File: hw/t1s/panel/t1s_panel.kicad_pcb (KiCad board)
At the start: 6 copper layers, 70 x 81 mm, 606 parts, among them J1 SFP edge (INF-8074i), J2 S2B-PH-K-S, U1 GW5AT-LV15MG132C1/I0, U2 GD25Q64CWIGR, U3 TPS62822DLC, U4 TPS22918DBVR, U5 LAN8670C2-E/LMX, U6 TLV75518PDBVR, U7 TLV75512PDBVR, U8 STM32G031F6P6, X1 OB2EL89CLIB112YLC-125M, Y1 25MHz CL12pF 2016

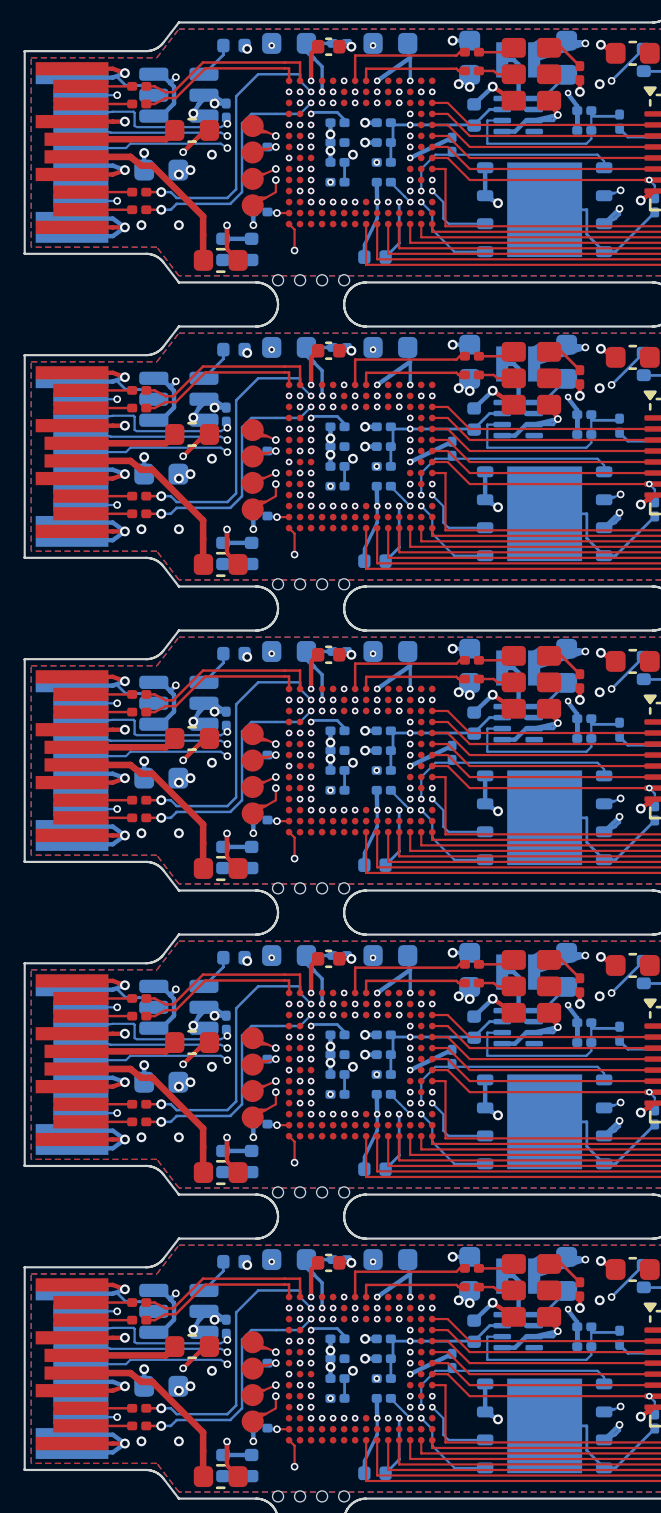
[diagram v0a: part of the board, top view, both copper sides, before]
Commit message: Review fixes: 100 V MDI DC block, 128 Mbit flash, T1S MDI geometry
- T1 C33/C34: 100 nF 100 V X5R 0402 (GRM155R62A104KE14D, C162178), split
  from the 16 V decap line (C1525) they had been grouped with
- T1 R6/R7: 1 k 1 % 0.2 W anti-surge 0402 (C313354) instead of 62.5 mW;
  still short of TI's 0.75 W 2010, documented
- T1S U2: GD25Q128EWIGR (C2982923), same WSON-8 footprint, so Gowin's
  default golden address 0x800000 is inside the part; ORDER.md gives the
  flash layout
- compliance.py: each lane's geometry comes from its routed track width;
  the T1S MDI is two 0.2 mm lines (Z0 44.8) with its own delay and loss,
  and an unsolved width now stops the run
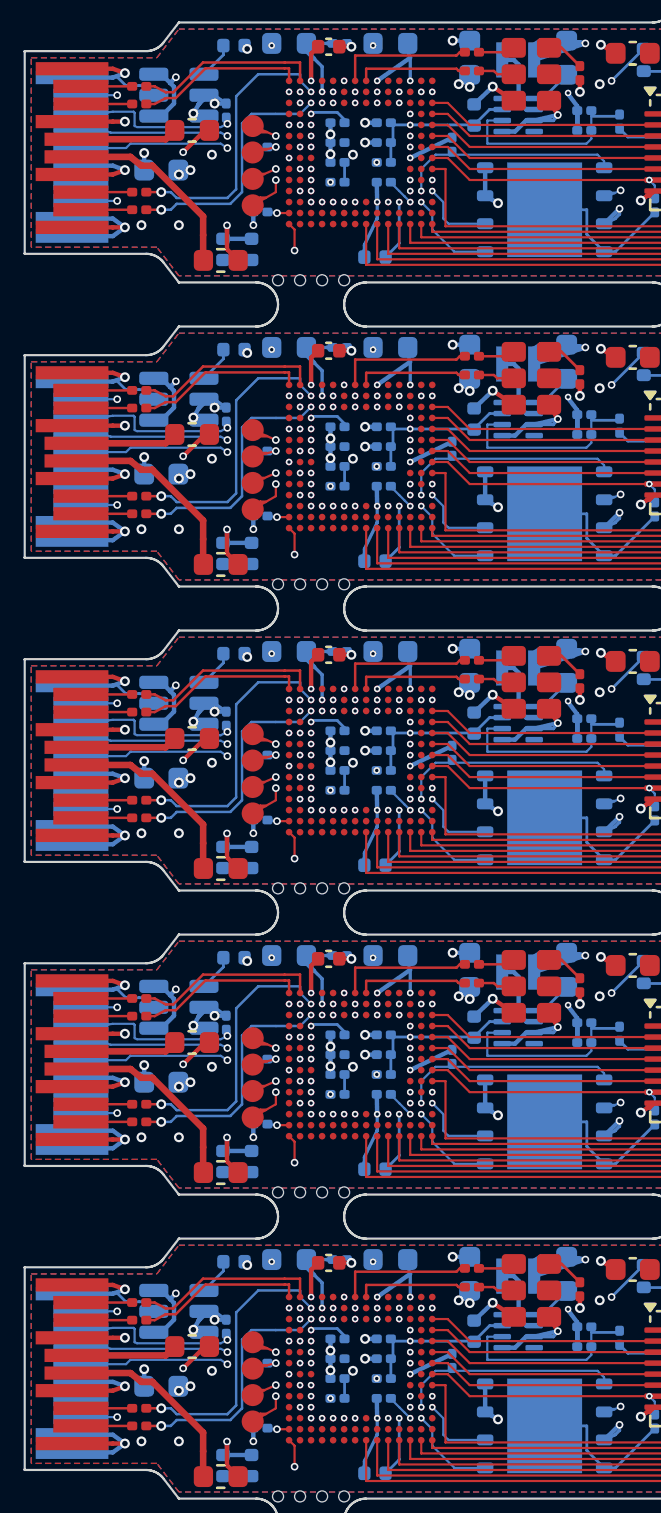
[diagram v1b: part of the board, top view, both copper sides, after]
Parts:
- U2 (x5): value GD25Q64CWIGR -> GD25Q128EWIGR
- moved KiKit_MB_31_4 24.0 mm to (125.0, 93.9)
- moved KiKit_MB_32_4 24.0 mm to (146.0, 82.3)
- moved KiKit_MB_10_4 24.0 mm to (125.0, 52.5)
- moved KiKit_MB_11_4 24.0 mm to (146.0, 40.9)
- moved KiKit_MB_3_4 24.0 mm to (125.0, 38.7)
- moved KiKit_MB_4_4 24.0 mm to (146.0, 27.1)
- moved KiKit_MB_17_4 24.0 mm to (125.0, 66.3)
- moved KiKit_MB_18_4 24.0 mm to (146.0, 54.7)
- moved KiKit_MB_24_4 24.0 mm to (125.0, 80.1)
- moved KiKit_MB_25_4 24.0 mm to (146.0, 68.5)
- moved KiKit_MB_31_3 22.3 mm to (126.0, 93.9)
- moved KiKit_MB_32_3 22.3 mm to (145.0, 82.3)
- moved KiKit_MB_10_3 22.3 mm to (126.0, 52.5)
- moved KiKit_MB_11_3 22.3 mm to (145.0, 40.9)
- moved KiKit_MB_3_3 22.3 mm to (126.0, 38.7)
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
